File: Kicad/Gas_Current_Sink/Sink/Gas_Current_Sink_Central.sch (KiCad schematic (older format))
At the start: 20 parts, among them J1 12V_input, J10 Xbee, J11 Xbee_SEL, J12 Xbee_pwr, J13 xbee_shield, J2 Current_pwr, J3 CO2_pwr, J4 CO2_pwr, J5 SD_card, J6 RTC, J7 Current_shield, J8 CO2_shield, J9 CO2_shield2, P1 Gas_Analog, P2 Current, P3 Gas_Digital, U1 LM7805_TO220, U2 LM337_TO220

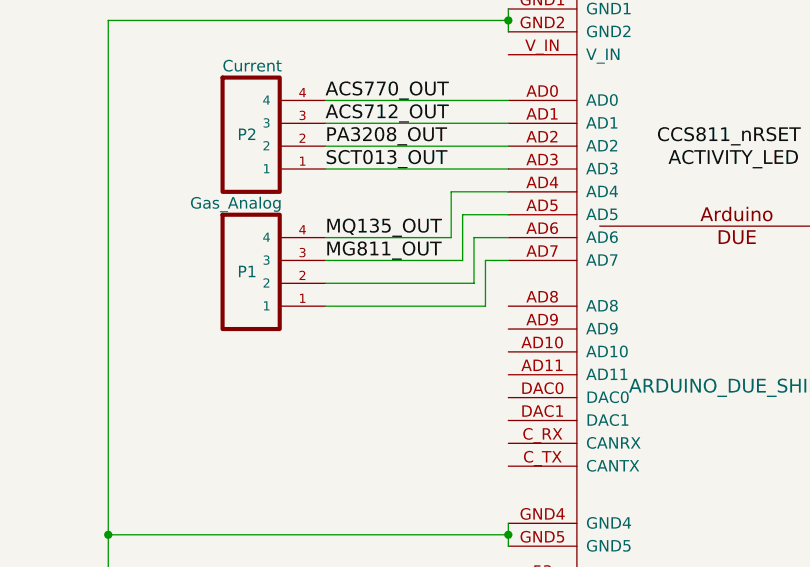
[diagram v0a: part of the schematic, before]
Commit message: Current and CO2 Arduino and Kicad Release 1.00! Added Arduino code for CO2 and Current sensor module. Updated Kicad projects for Arduino Due shield and top of the box CO2 PCB.
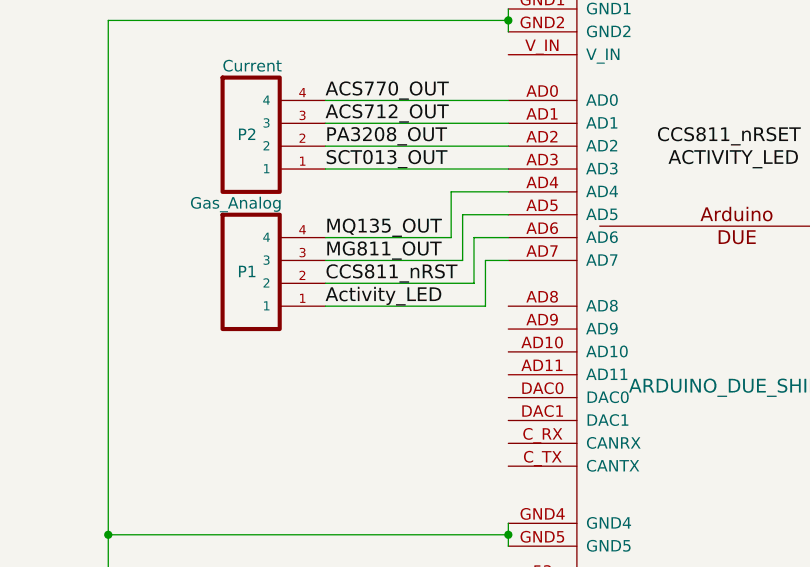
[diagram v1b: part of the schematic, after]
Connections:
- net CCS811_nRST: now reaches P1.2, SHIELD1.AD6
- net Activity_LED: now reaches P1.1, SHIELD1.AD7
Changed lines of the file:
@@
 	5750 7400 5750 7550
 Connection ~ 5750 7550
+Text Label 3850 3500 0    60   ~ 0
+Activity_LED
+Text Label 3850 3400 0    60   ~ 0
+CCS811_nRST
 $EndSCHEMATC
